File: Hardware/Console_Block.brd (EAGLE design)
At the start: 30.5 x 44.5 mm, 41 parts, among them Q1 BSS138, U2 FTS31XS-U, U4 TPS62065

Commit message: Ready for reds Tweaked silk positions, add some restrict between pads on QFN No known to-do items
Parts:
- U2: value FTS31XS-U -> FT231XS-U
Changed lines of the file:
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@@
 <setting verticaltext="up"/>
 </settings>
-<grid distance="0.01" unitdist="inch" unit="inch" style="lines" multiple="1" display="yes" altdistance="0.005" altunitdist="inch" altunit="inch"/>
+<grid distance="0.05" unitdist="inch" unit="inch" style="lines" multiple="1" display="yes" altdistance="0.005" altunitdist="inch" altunit="inch"/>
 <layers>
 <layer number="1" name="Top" color="4" fill="1" visible="yes" active="yes"/>
@@
 <text x="1.016" y="28.702" size="1.016" layer="21" font="vector" ratio="15" rot="SR270" align="center">RX</text>
 <text x="1.016" y="23.749" size="1.016" layer="21" font="vector" ratio="15" rot="SR270" align="center">TX</text>
-<text x="0.762" y="17.018" size="1.016" layer="21" font="vector" ratio="15" rot="SR270">POWER</text>
+<text x="1.016" y="16.891" size="1.016" layer="21" font="vector" ratio="15" rot="SR270" align="center-left">POWER</text>
 <text x="30.099" y="3.81" size="1.016" layer="1" font="vector" ratio="15" rot="R90">v10</text>
 <text x="29.972" y="26.416" size="1.27" layer="21" font="vector" ratio="15" rot="R90">Console Block</text>
@@
 <wire x1="24.003" y1="23.368" x2="24.003" y2="22.0345" width="0.127" layer="42"/>
 <wire x1="24.003" y1="22.0345" x2="24.003" y2="23.368" width="0.127" layer="41"/>
+<wire x1="13.208" y1="14.224" x2="13.208" y2="13.843" width="0.1524" layer="41"/>
+<wire x1="11.684" y1="14.224" x2="11.684" y2="13.843" width="0.1524" layer="41"/>
 </plain>
 <attributes>
@@
 <attribute name="PROD_ID" value="CONN-11752" x="15.24" y="42.418" size="1.778" layer="27" rot="R270" display="off"/>
 </element>
-<element name="U2" library="SparkFun-DigitalIC" package="SSOP20_L" value="FTS31XS-U" x="15.24" y="30.226" rot="R90">
+<element name="U2" library="SparkFun-DigitalIC" package="SSOP20_L" value="FT231XS-U" x="15.24" y="30.226" rot="R90">
 <attribute name="PROD_ID" value="IC-11524" x="15.24" y="30.226" size="1.778" layer="27" rot="R90" display="off"/>
 </element>

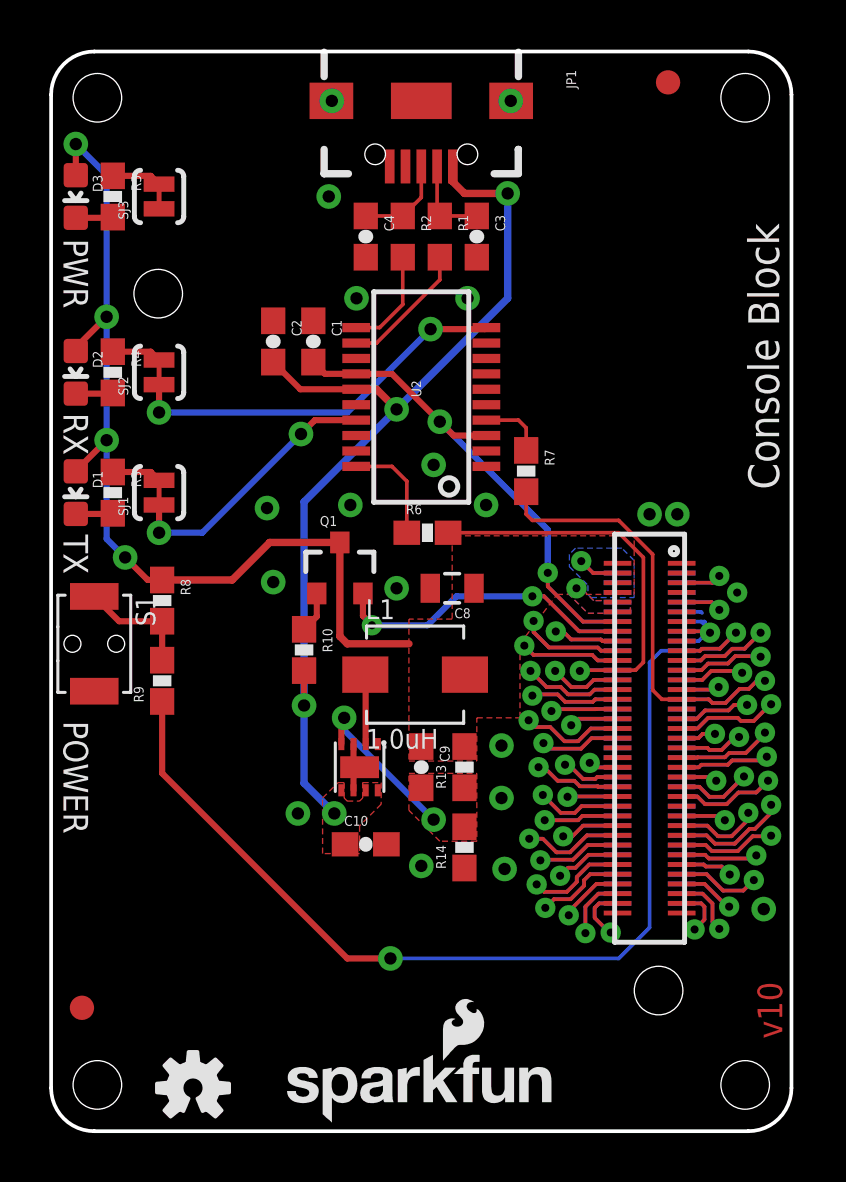
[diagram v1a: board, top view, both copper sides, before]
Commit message: added bottom side fiducials
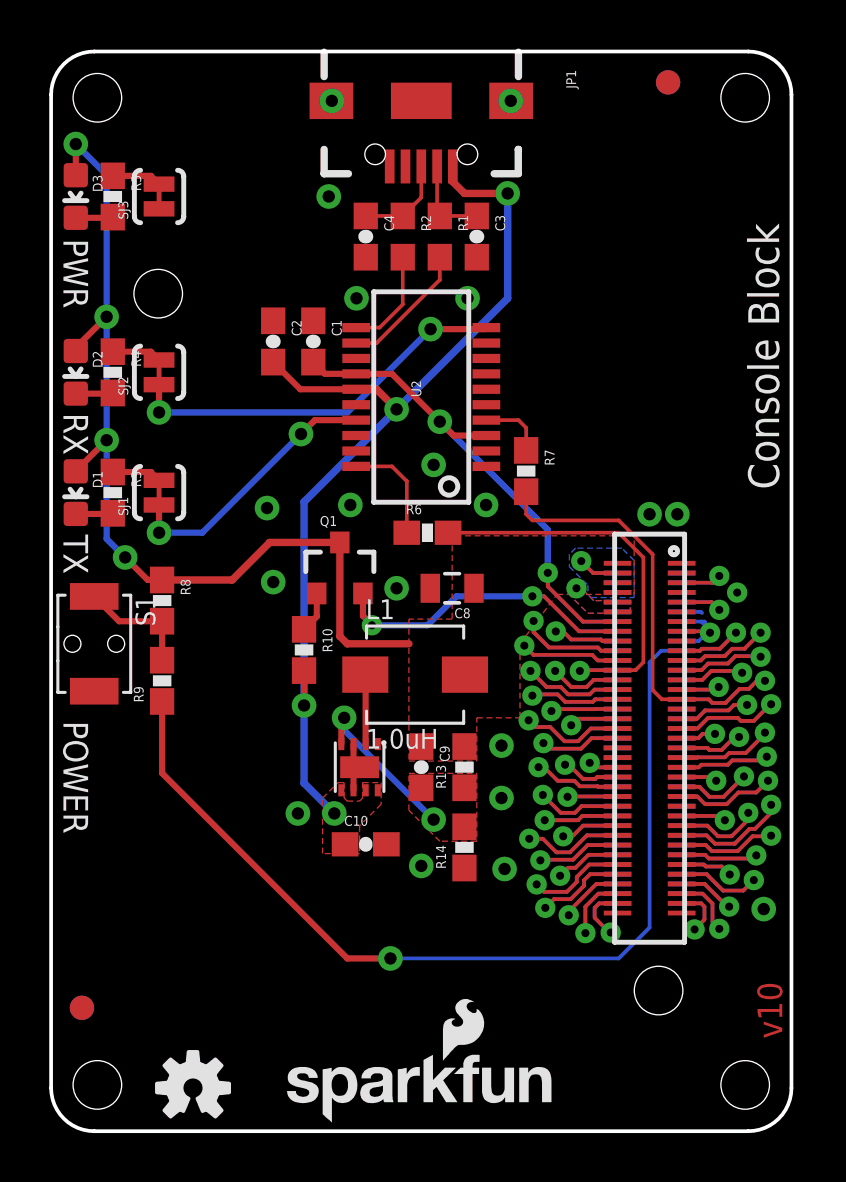
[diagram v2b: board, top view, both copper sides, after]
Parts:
- added FID3, FID4: FIDUCIAL1X2, SparkFun-Aesthetics:FIDUCIAL-1X2
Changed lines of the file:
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@@
 <setting verticaltext="up"/>
 </settings>
-<grid distance="0.05" unitdist="inch" unit="inch" style="lines" multiple="1" display="yes" altdistance="0.005" altunitdist="inch" altunit="inch"/>
+<grid distance="0.05" unitdist="inch" unit="inch" style="lines" multiple="1" display="yes" altdistance="0.01" altunitdist="inch" altunit="inch"/>
 <layers>
 <layer number="1" name="Top" color="4" fill="1" visible="yes" active="yes"/>
-<layer number="2" name="Route2" color="1" fill="3" visible="no" active="yes"/>
-<layer number="15" name="Route15" color="4" fill="6" visible="no" active="yes"/>
+<layer number="2" name="Route2" color="1" fill="3" visible="yes" active="yes"/>
+<layer number="15" name="Route15" color="4" fill="6" visible="yes" active="yes"/>
 <layer number="16" name="Bottom" color="1" fill="1" visible="yes" active="yes"/>
 <layer number="17" name="Pads" color="2" fill="1" visible="yes" active="yes"/>
 <layer number="18" name="Vias" color="2" fill="1" visible="yes" active="yes"/>
 <layer number="19" name="Unrouted" color="6" fill="1" visible="yes" active="yes"/>
-<layer number="20" name="Dimension" color="15" fill="1" visible="yes" active="yes"/>
-<layer number="21" name="tPlace" color="16" fill="1" visible="yes" active="yes"/>
-<layer number="22" name="bPlace" color="14" fill="1" visible="yes" active="yes"/>
+<layer number="20" name="Dimension" color="6" fill="1" visible="yes" active="yes"/>
+<layer number="21" name="tPlace" color="6" fill="1" visible="yes" active="yes"/>
+<layer number="22" name="bPlace" color="6" fill="1" visible="yes" active="yes"/>
 <layer number="23" name="tOrigins" color="15" fill="1" visible="yes" active="yes"/>
 <layer number="24" name="bOrigins" color="15" fill="1" visible="yes" active="yes"/>
-<layer number="25" name="tNames" color="7" fill="1" visible="no" active="yes"/>
-<layer number="26" name="bNames" color="7" fill="1" visible="no" active="yes"/>
-<layer number="27" name="tValues" color="7" fill="1" visible="no" active="yes"/>
-<layer number="28" name="bValues" color="7" fill="1" visible="no" active="yes"/>
-<layer number="29" name="tStop" color="7" fill="3" visible="no" active="yes"/>
-<layer number="30" name="bStop" color="7" fill="6" visible="no" active="yes"/>
-<layer number="31" name="tCream" color="7" fill="4" visible="no" active="yes"/>
-<layer number="32" name="bCream" color="7" fill="5" visible="no" active="yes"/>
-<layer number="39" name="tKeepout" color="4" fill="11" visible="no" active="yes"/>
-<layer number="40" name="bKeepout" color="1" fill="11" visible="no" active="yes"/>
-<layer number="41" name="tRestrict" color="4" fill="10" visible="no" active="yes"/>
-<layer number="42" name="bRestrict" color="1" fill="10" visible="no" active="yes"/>
-<layer number="43" name="vRestrict" color="2" fill="10" visible="no" active="yes"/>
-<layer number="44" name="Drills" color="7" fill="1" visible="no" active="yes"/>
+<layer number="25" name="tNames" color="7" fill="1" visible="yes" active="yes"/>
+<layer number="26" name="bNames" color="7" fill="1" visible="yes" active="yes"/>
+<layer number="27" name="tValues" color="7" fill="1" visible="yes" active="yes"/>
+<layer number="28" name="bValues" color="7" fill="1" visible="yes" active="yes"/>
+<layer number="29" name="tStop" color="7" fill="3" visible="yes" active="yes"/>
+<layer number="30" name="bStop" color="7" fill="6" visible="yes" active="yes"/>
+<layer number="31" name="tCream" color="7" fill="4" visible="yes" active="yes"/>
+<layer number="32" name="bCream" color="7" fill="5" visible="yes" active="yes"/>
+<layer number="39" name="tKeepout" color="4" fill="11" visible="yes" active="yes"/>
+<layer number="40" name="bKeepout" color="1" fill="11" visible="yes" active="yes"/>
+<layer number="41" name="tRestrict" color="4" fill="10" visible="yes" active="yes"/>
+<layer number="42" name="bRestrict" color="1" fill="10" visible="yes" active="yes"/>
+<layer number="43" name="vRestrict" color="2" fill="10" visible="yes" active="yes"/>
+<layer number="44" name="Drills" color="7" fill="1" visible="yes" active="yes"/>
 <layer number="45" name="Holes" color="7" fill="1" visible="yes" active="yes"/>
-<layer number="46" name="Milling" color="3" fill="1" visible="no" active="yes"/>
+<layer number="46" name="Milling" color="3" fill="1" visible="yes" active="yes"/>
 <layer number="51" name="tDocu" color="6" fill="1" visible="yes" active="yes"/>
 <layer number="3" name="Route3" color="4" fill="3" visible="no" active="no"/>
@@
 <attribute name="PROD_ID" value="RES-07856" x="10.414" y="19.812" size="1.778" layer="27" rot="R270" display="off"/>
 </element>
+<element name="FID3" library="SparkFun-Aesthetics" package="FIDUCIAL-1X2" value="FIDUCIAL1X2" x="1.27" y="5.08" rot="MR0"/>
+<element name="FID4" library="SparkFun-Aesthetics" package="FIDUCIAL-1X2" value="FIDUCIAL1X2" x="25.4" y="43.18" rot="MR0"/>
 </elements>
 <signals>
